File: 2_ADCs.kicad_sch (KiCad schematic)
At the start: 38 parts

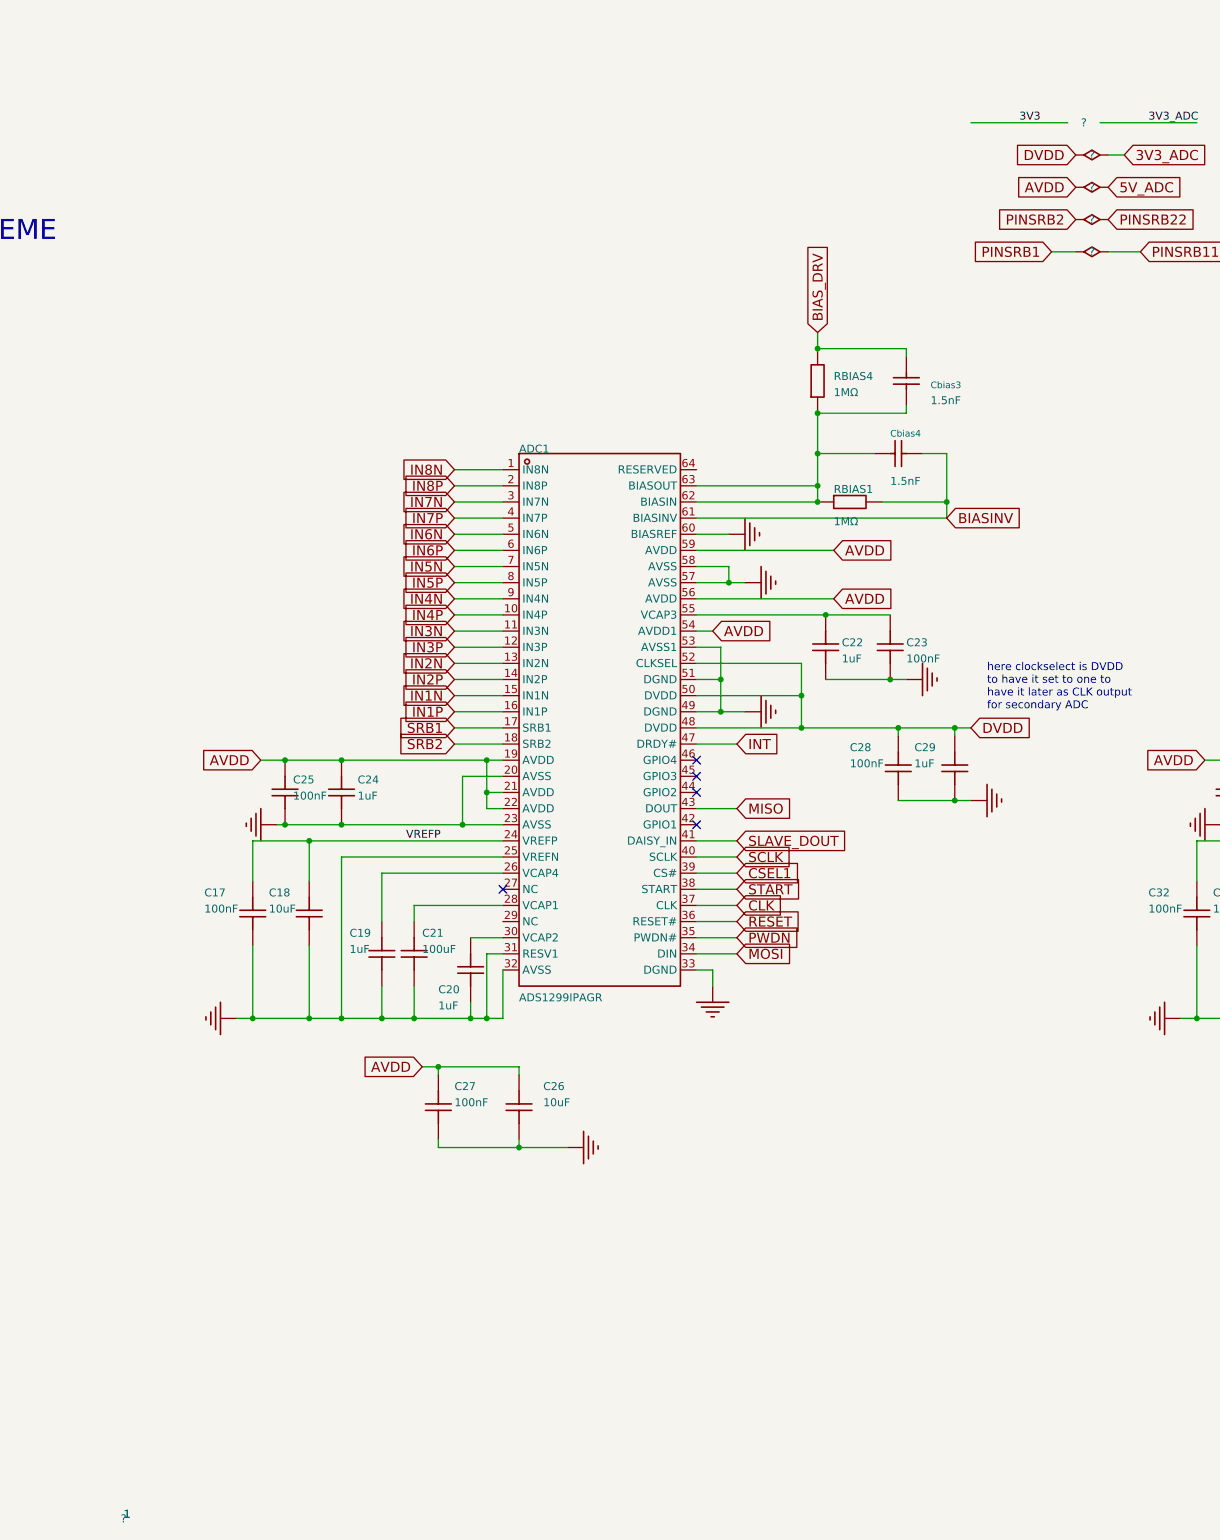
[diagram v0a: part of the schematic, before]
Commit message: Fix import2 ERC: pin types, references, and NC pins
- Convert EasyEDA R/C input pins to passive in lib_symbols and symbol library
- Set targeted pin types for ESP32-C6, TYPE-C, ADS1299 NC, TPD4E1B06, TPS62821
- Annotate Short-Symbol jumpers (JP1-6), sheet frames (F1-F2), and #PWR flags
- ERC: 576 violations / 122 errors -> 448 violations / 4 errors
- Net names unchanged; remaining errors are BIASIN/BIASOUT wiring and GND PWR_FLAG
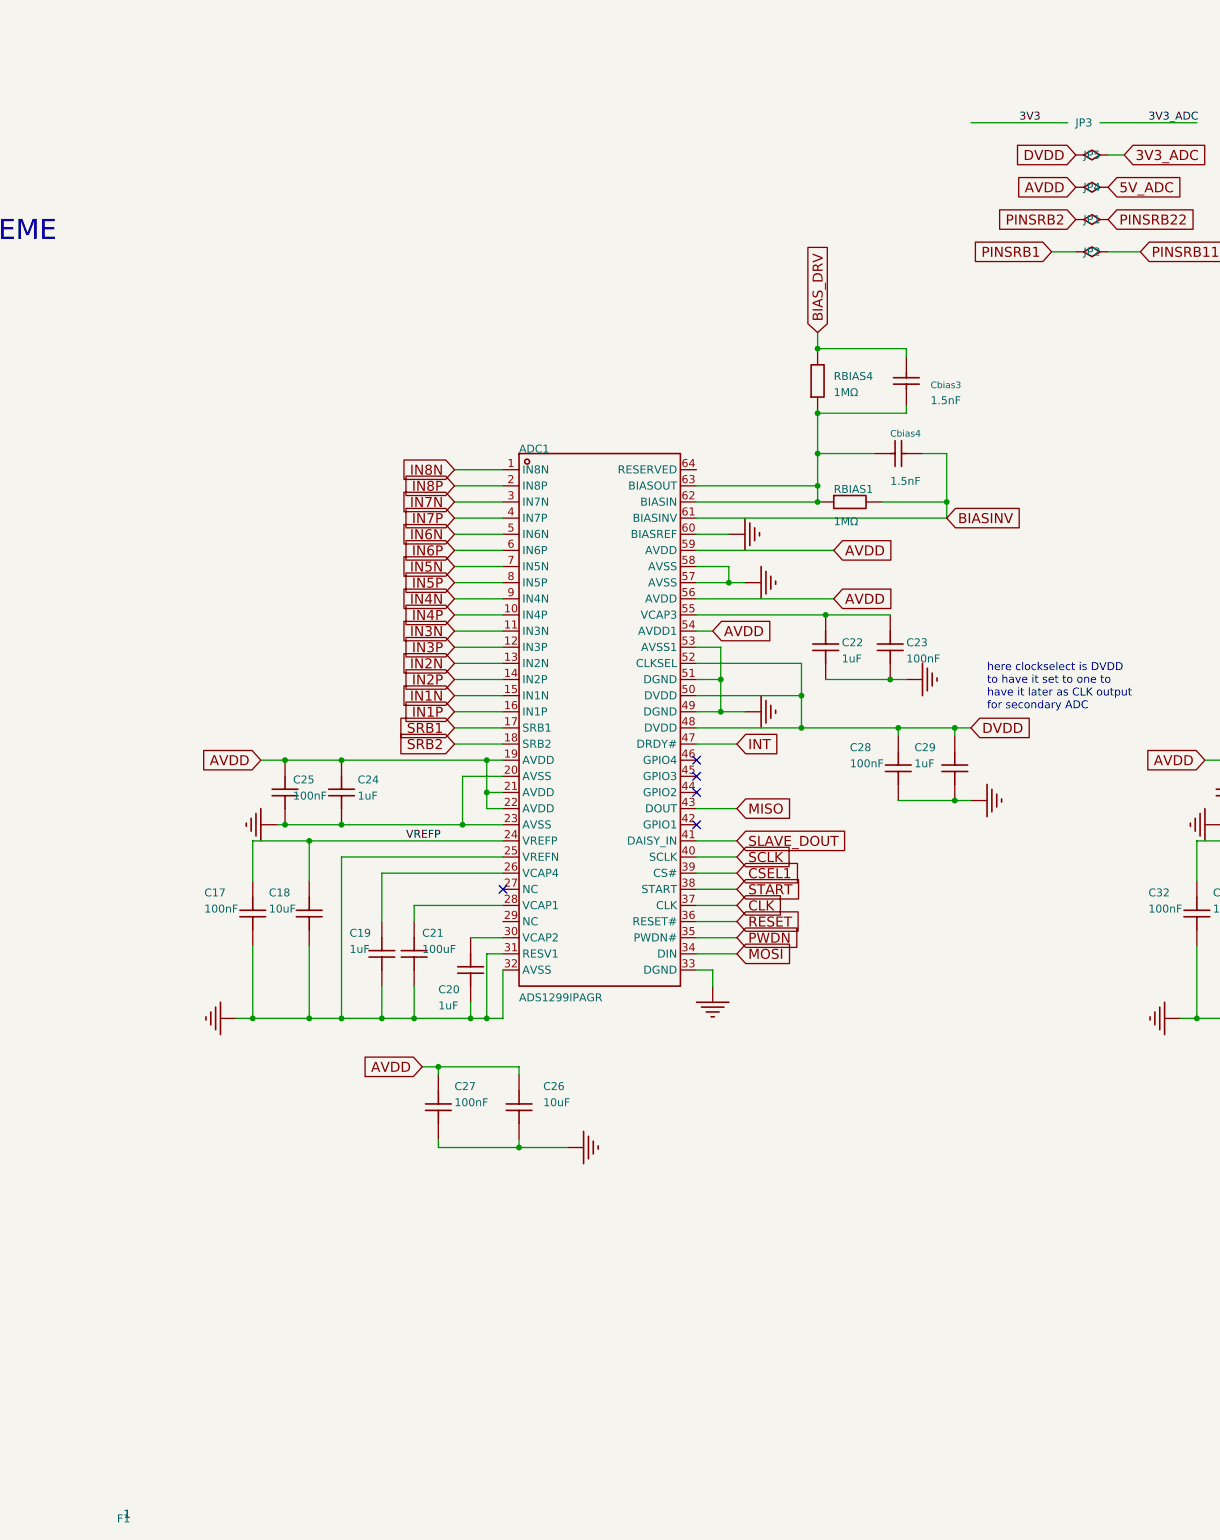
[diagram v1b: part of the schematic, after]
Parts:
- F1: renamed from ?; now left out of the parts list
- gave numbers to parts that had none: 5
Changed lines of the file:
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@@
 		(in_pos_files yes)
 		(dnp no)
-		(property "Reference" "#PWR?"
+		(property "Reference" "#PWR01"
 			(at 331.47 142.24 0)
 			(hide yes)
@@
 			(project "import2"
 				(path "/06cae45c-d474-473f-93a9-05a684cc4e1b/1b8a5fce-a845-4467-ac27-03cf9cf28f5f"
-					(reference "#PWR?")
+					(reference "#PWR02")
 					(unit 1)
 				)
@@
 		(in_pos_files yes)
 		(dnp no)
-		(property "Reference" "#PWR?"
+		(property "Reference" "#PWR03"
 			(at 328.93 213.36 0)
 			(hide yes)
@@
 			(project "import2"
 				(path "/06cae45c-d474-473f-93a9-05a684cc4e1b/1b8a5fce-a845-4467-ac27-03cf9cf28f5f"
-					(reference "#PWR?")
+					(reference "#PWR04")
 					(unit 1)
 				)
@@
 		(in_pos_files yes)
 		(dnp no)
-		(property "Reference" "#PWR?"
+		(property "Reference" "#PWR05"
 			(at 185.42 170.18 0)
 			(hide yes)
@@
 			(project "import2"
 				(path "/06cae45c-d474-473f-93a9-05a684cc4e1b/1b8a5fce-a845-4467-ac27-03cf9cf28f5f"
-					(reference "#PWR?")
+					(reference "#PWR06")
 					(unit 1)
 				)
@@
 		(in_pos_files yes)
 		(dnp no)
-		(property "Reference" "#PWR?"
+		(property "Reference" "#PWR07"
 			(at 111.76 187.96 0)
 			(hide yes)
@@
 			(project "import2"
 				(path "/06cae45c-d474-473f-93a9-05a684cc4e1b/1b8a5fce-a845-4467-ac27-03cf9cf28f5f"
-					(reference "#PWR?")
+					(reference "#PWR08")
 					(unit 1)
 				)
@@
 		(in_pos_files yes)
 		(dnp no)
-		(property "Reference" "#PWR?"
+		(property "Reference" "#PWR09"
 			(at 334.01 162.56 0)
 			(hide yes)
@@
 			(project "import2"
 				(path "/06cae45c-d474-473f-93a9-05a684cc4e1b/1b8a5fce-a845-4467-ac27-03cf9cf28f5f"
-					(reference "#PWR?")
+					(reference "#PWR10")
 					(unit 1)
 				)
@@
 		(in_pos_files yes)
 		(dnp no)
-		(property "Reference" "#PWR?"
+		(property "Reference" "#PWR11"
 			(at 369.57 184.15 0)
 			(hide yes)
@@
 			(project "import2"
 				(path "/06cae45c-d474-473f-93a9-05a684cc4e1b/1b8a5fce-a845-4467-ac27-03cf9cf28f5f"
-					(reference "#PWR?")
+					(reference "#PWR12")
 					(unit 1)
 				)
@@
 		(in_pos_files yes)
 		(dnp no)
-		(property "Reference" "?"
+		(property "Reference" "JP1"
 			(at 240.03 92.71 0)
 			(show_name no)
@@
 			(project "import2"
 				(path "/06cae45c-d474-473f-93a9-05a684cc4e1b/1b8a5fce-a845-4467-ac27-03cf9cf28f5f"
-					(reference "?")
+					(reference "JP1")
 					(unit 1)
 				)
@@
 		(in_pos_files yes)
 		(dnp no)
-		(property "Reference" "?"
+		(property "Reference" "JP2"
 			(at 240.03 97.79 0)
 			(show_name no)
@@
 			(project "import2"
 				(path "/06cae45c-d474-473f-93a9-05a684cc4e1b/1b8a5fce-a845-4467-ac27-03cf9cf28f5f"
-					(reference "?")
+					(reference "JP2")
 					(unit 1)
 				)
@@
 		(in_pos_files yes)
 		(dnp no)
-		(property "Reference" "#PWR?"
+		(property "Reference" "#PWR13"
 			(at 210.82 165.1 0)
 			(hide yes)
@@
 			(project "import2"
 				(path "/06cae45c-d474-473f-93a9-05a684cc4e1b/1b8a5fce-a845-4467-ac27-03cf9cf28f5f"
-					(reference "#PWR?")
+					(reference "#PWR14")
 					(unit 1)
 				)
@@
 		(in_pos_files yes)
 		(dnp no)
-		(property "Reference" "#PWR?"
+		(property "Reference" "#PWR15"
 			(at 359.41 165.1 0)
 			(hide yes)
@@
 			(project "import2"
 				(path "/06cae45c-d474-473f-93a9-05a684cc4e1b/1b8a5fce-a845-4467-ac27-03cf9cf28f5f"
-					(reference "#PWR?")
+					(reference "#PWR16")
 					(unit 1)
 				)
@@
 		(in_pos_files yes)
 		(dnp no)
-		(property "Reference" "?"
+		(property "Reference" "JP3"
 			(at 238.76 77.47 0)
 			(show_name no)
@@
 			(project "import2"
 				(path "/06cae45c-d474-473f-93a9-05a684cc4e1b/1b8a5fce-a845-4467-ac27-03cf9cf28f5f"
-					(reference "?")
+					(reference "JP3")
 					(unit 0)
 				)
@@
 		(in_pos_files yes)
 		(dnp no)
-		(property "Reference" "#PWR?"
+		(property "Reference" "#PWR17"
 			(at 182.88 142.24 0)
 			(hide yes)
@@
 			(project "import2"
 				(path "/06cae45c-d474-473f-93a9-05a684cc4e1b/1b8a5fce-a845-4467-ac27-03cf9cf28f5f"
-					(reference "#PWR?")
+					(reference "#PWR18")
 					(unit 1)
 				)
@@
 		(in_pos_files yes)
 		(dnp no)
-		(property "Reference" "?"
+		(property "Reference" "JP4"
 			(at 240.03 87.63 0)
 			(show_name no)
@@
 			(project "import2"
 				(path "/06cae45c-d474-473f-93a9-05a684cc4e1b/1b8a5fce-a845-4467-ac27-03cf9cf28f5f"
-					(reference "?")
+					(reference "JP4")
 					(unit 1)
 				)
@@
 		(in_pos_files yes)
 		(dnp no)
-		(property "Reference" "#PWR?"
+		(property "Reference" "#PWR19"
 			(at 157.48 238.76 0)
 			(hide yes)
@@
 			(project "import2"
 				(path "/06cae45c-d474-473f-93a9-05a684cc4e1b/1b8a5fce-a845-4467-ac27-03cf9cf28f5f"
-					(reference "#PWR?")
+					(reference "#PWR20")
 					(unit 1)
 				)
@@
 		(in_pos_files yes)
 		(dnp no)
-		(property "Reference" "?"
+		(property "Reference" "JP5"
 			(at 240.03 82.55 0)
 			(show_name no)
@@
 			(project "import2"
 				(path "/06cae45c-d474-473f-93a9-05a684cc4e1b/1b8a5fce-a845-4467-ac27-03cf9cf28f5f"
-					(reference "?")
+					(reference "JP5")
 					(unit 1)
 				)
@@
 		(in_pos_files yes)
 		(dnp no)
-		(property "Reference" "#PWR?"
+		(property "Reference" "#PWR21"
 			(at 220.98 184.15 0)
 			(hide yes)
@@
 			(project "import2"
 				(path "/06cae45c-d474-473f-93a9-05a684cc4e1b/1b8a5fce-a845-4467-ac27-03cf9cf28f5f"
-					(reference "#PWR?")
+					(reference "#PWR22")
 					(unit 1)
 				)
@@
 		(body_style 0)
 		(exclude_from_sim no)
-		(in_bom yes)
-		(on_board yes)
+		(in_bom no)
+		(on_board no)
 		(in_pos_files yes)
 		(dnp no)
-		(property "Reference" "?"
+		(property "Reference" "F1"
 			(at 87.63 297.18 0)
 			(show_name no)
@@
 			(project "import2"
 				(path "/06cae45c-d474-473f-93a9-05a684cc4e1b/1b8a5fce-a845-4467-ac27-03cf9cf28f5f"
-					(reference "?")
+					(reference "F1")
 					(unit 0)
 				)
@@
 		(in_pos_files yes)
 		(dnp no)
-		(property "Reference" "#PWR?"
+		(property "Reference" "#PWR23"
 			(at 334.01 170.18 0)
 			(hide yes)
@@
 			(project "import2"
 				(path "/06cae45c-d474-473f-93a9-05a684cc4e1b/1b8a5fce-a845-4467-ac27-03cf9cf28f5f"
-					(reference "#PWR?")
+					(reference "#PWR24")
 					(unit 1)
 				)
@@
 		(in_pos_files yes)
 		(dnp no)
-		(property "Reference" "#PWR?"
+		(property "Reference" "#PWR25"
 			(at 334.01 149.86 0)
 			(hide yes)
@@
 			(project "import2"
 				(path "/06cae45c-d474-473f-93a9-05a684cc4e1b/1b8a5fce-a845-4467-ac27-03cf9cf28f5f"
-					(reference "#PWR?")
+					(reference "#PWR26")
 					(unit 1)
 				)
@@
 		(in_pos_files yes)
 		(dnp no)
-		(property "Reference" "#PWR?"
+		(property "Reference" "#PWR27"
 			(at 260.35 187.96 0)
 			(hide yes)
@@
 			(project "import2"
 				(path "/06cae45c-d474-473f-93a9-05a684cc4e1b/1b8a5fce-a845-4467-ac27-03cf9cf28f5f"
-					(reference "#PWR?")
+					(reference "#PWR28")
 					(unit 1)
 				)
@@
 		(in_pos_files yes)
 		(dnp no)
-		(property "Reference" "#PWR?"
+		(property "Reference" "#PWR29"
 			(at 185.42 149.86 0)
 			(hide yes)
@@
 			(project "import2"
 				(path "/06cae45c-d474-473f-93a9-05a684cc4e1b/1b8a5fce-a845-4467-ac27-03cf9cf28f5f"
-					(reference "#PWR?")
+					(reference "#PWR30")
 					(unit 1)
 				)
@@
 		(in_pos_files yes)
 		(dnp no)
-		(property "Reference" "#PWR?"
+		(property "Reference" "#PWR31"
 			(at 332.74 190.5 0)
 			(hide yes)
@@
 			(project "import2"
 				(path "/06cae45c-d474-473f-93a9-05a684cc4e1b/1b8a5fce-a845-4467-ac27-03cf9cf28f5f"
-					(reference "#PWR?")
+					(reference "#PWR32")
 					(unit 1)
 				)
@@
 		(in_pos_files yes)
 		(dnp no)
-		(property "Reference" "#PWR?"
+		(property "Reference" "#PWR33"
 			(at 306.07 238.76 0)
 			(hide yes)
@@
 			(project "import2"
 				(path "/06cae45c-d474-473f-93a9-05a684cc4e1b/1b8a5fce-a845-4467-ac27-03cf9cf28f5f"
-					(reference "#PWR?")
+					(reference "#PWR34")
 					(unit 1)
 				)
@@
 		(in_pos_files yes)
 		(dnp no)
-		(property "Reference" "#PWR?"
+		(property "Reference" "#PWR35"
 			(at 105.41 218.44 0)
 			(hide yes)
@@
 			(project "import2"
 				(path "/06cae45c-d474-473f-93a9-05a684cc4e1b/1b8a5fce-a845-4467-ac27-03cf9cf28f5f"
-					(reference "#PWR?")
+					(reference "#PWR36")
 					(unit 1)
 				)

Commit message: Fix ERC
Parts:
- removed F1: (no value), ProPrj_BCI-easyedapro:, symbol ProPrj_BCI-easyedapro:Sheet-Symbol_A4
- removed JP1, JP2, JP4, JP5: (no value), ProPrj_BCI-easyedapro:, symbol ProPrj_BCI-easyedapro:Short-Symbol
- removed JP3: (no value), ProPrj_BCI-easyedapro:, symbol ProPrj_BCI-easyedapro:Short-Symbol-Auto
- added NT1, NT2, NT3, NT4: NetTie_2, symbol Device:NetTie_2
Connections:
- net 3V3_ADC: now also NT4.2
- net 5V_ADC: now also NT3.2
- net AVDD: now also NT3.1
- net DVDD: now also NT4.1
- net PINSRB1: now also NT1.1
- net PINSRB11: now also NT1.2
- net PINSRB2: now also NT2.1
- net PINSRB22: now also NT2.2
- no-connect marks 12 -> 15

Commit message: PCB update. DRC <300
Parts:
- added NT5: NetTie_2, NetTie:NetTie-2_SMD_Pad2.0mm, symbol Device:NetTie_2
- NT1, NT2, NT3, NT4: footprint (none) -> NetTie:NetTie-2_SMD_Pad2.0mm
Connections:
- net GND: now also NT5.2; no longer ADC1.20 (AVSS), ADC1.23 (AVSS), ADC1.25 (VREFN), ADC1.31 (RESV1), ADC1.32 (AVSS), C17.1, C18.1, C19.2, C20.1, C21.2, C24.1, C25.1, C26.1, C27.1
- new net AVSS: ADC1.20 (AVSS), ADC1.23 (AVSS), ADC1.25 (VREFN), ADC1.31 (RESV1), ADC1.32 (AVSS), C17.1, C18.1, C19.2, C20.1, C21.2, C24.1, C25.1, C26.1, C27.1, NT5.1
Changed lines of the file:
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@@
 		)
 	)
+	(global_label "GND"
+		(shape input)
+		(at 242.57 76.2 0)
+		(effects
+			(font
+				(size 1.5748 1.5748)
+			)
+			(justify left)
+		)
+		(property "Intersheetrefs" "${INTERSHEET_REFS}"
+			(at 242.57 76.2 0)
+			(hide yes)
+			(show_name no)
+			(do_not_autoplace no)
+			(effects
+				(font
+					(size 1.27 1.27)
+				)
+			)
+		)
+	)
 	(global_label "AVDD"
 		(shape input)
@@
 		)
 	)
+	(global_label "AVSS"
+		(shape input)
+		(at 237.49 76.2 180)
+		(effects
+			(font
+				(size 1.5748 1.5748)
+			)
+			(justify right)
+		)
+		(property "Intersheetrefs" "${INTERSHEET_REFS}"
+			(at 237.49 76.2 0)
+			(hide yes)
+			(show_name no)
+			(do_not_autoplace no)
+			(effects
+				(font
+					(size 1.27 1.27)
+				)
+			)
+		)
+	)
 	(global_label "AVDD"
 		(shape input)
@@
 	)
 	(symbol
+		(lib_id "Device:NetTie_2")
+		(at 240.03 76.2 0)
+		(unit 1)
+		(body_style 1)
+		(exclude_from_sim no)
+		(in_bom no)
+		(on_board yes)
+		(in_pos_files yes)
+		(dnp no)
+		(property "Reference" "NT5"
+			(at 240.284 76.2 0)
+			(show_name no)
+			(do_not_autoplace no)
+			(effects
+				(font
+					(size 1.27 1.27)
+				)
+			)
+		)
+		(property "Value" "NetTie_2"
+			(at 240.03 77.724 0)
+			(hide yes)
+			(show_name no)
+			(do_not_autoplace no)
+			(effects
+				(font
+					(size 1.27 1.27)
+				)
+			)
+		)
+		(property "Footprint" "NetTie:NetTie-2_SMD_Pad2.0mm"
+			(at 240.03 76.2 0)
+			(hide yes)
+			(show_name no)
+			(do_not_autoplace no)
+			(effects
+				(font
+					(size 1.27 1.27)
+				)
+			)
+		)
+		(property "Datasheet" ""
+			(at 240.03 76.2 0)
+			(hide yes)
+			(show_name no)
+			(do_not_autoplace no)
+			(effects
+				(font
+					(size 1.27 1.27)
+				)
+			)
+		)
+		(property "Description" "Net tie, 2 pins"
+			(at 240.03 76.2 0)
+			(hide yes)
+			(show_name no)
+			(do_not_autoplace no)
+			(effects
+				(font
+					(size 1.27 1.27)
+				)
+			)
+		)
+		(pin "2"
+		)
+		(pin "1"
+		)
+		(instances
+			(project "import2"
+				(path "/06cae45c-d474-473f-93a9-05a684cc4e1b/1b8a5fce-a845-4467-ac27-03cf9cf28f5f"
+					(reference "NT5")
+					(unit 1)
+				)
+			)
+		)
+	)
+	(symbol
 		(lib_id "ProPrj_BCI-easyedapro:GRM188R71H104KA93D")
 		(at 261.62 182.88 90)
@@
 			)
 		)
-		(property "Value" "GND"
+		(property "Value" "AVSS"
 			(at 111.76 187.96 0)
 			(hide yes)
@@
 			)
 		)
-		(property "Footprint" ""
+		(property "Footprint" "NetTie:NetTie-2_SMD_Pad2.0mm"
 			(at 240.03 87.63 0)
 			(hide yes)
@@
 			)
 		)
-		(property "Footprint" ""
+		(property "Footprint" "NetTie:NetTie-2_SMD_Pad2.0mm"
 			(at 240.03 92.71 0)
 			(hide yes)
@@
 			)
 		)
-		(property "Value" "GND"
+		(property "Value" "AVSS"
 			(at 157.48 238.76 0)
 			(hide yes)
@@
 			)
 		)
-		(property "Footprint" ""
+		(property "Footprint" "NetTie:NetTie-2_SMD_Pad2.0mm"
 			(at 241.3 97.79 0)
 			(hide yes)
@@
 			)
 		)
-		(property "Footprint" ""
+		(property "Footprint" "NetTie:NetTie-2_SMD_Pad2.0mm"
 			(at 241.3 82.55 0)
 			(hide yes)
@@
 			)
 		)
-		(property "Value" "GND"
+		(property "Value" "AVSS"
 			(at 105.41 218.44 0)
 			(hide yes)
